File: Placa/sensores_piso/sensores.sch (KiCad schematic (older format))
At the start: 10 parts, among them P1 CONN_8X2, U1 CNY70, U2 CNY70

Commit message: arreglo placa sensores
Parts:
- removed P1: CONN_8X2, ~, symbol CONN_8X2
- removed R_sens1, R_sens2, R_sens3: 200, symbol R
- added P1: CONN_5X2, ~, symbol CONN_5X2
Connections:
- net S3+ is gone; now on net 5V: U2.C (COL)
- net Vcc is gone; now on net 5V: ??1.C (COL)
- net GND: now also RV2.3, RV3.3, P1.10
- net Vcc sensor piso izquierda: now reaches ??1.A
- net Vcc sensor piso izquierda: now also P1.4
- net Vcc sensor piso centro: now reaches U1.A
- net Vcc sensor piso centro: now also P1.6
- net Vcc sensor piso derecha: now reaches U2.A
- net Vcc sensor piso derecha: now also P1.2
- net S- renamed GND LED sensores
- net GND LED sensores: now also P1.8; no longer RV2.3, RV3.3
- net S1+ renamed 5V
- net 5V: now also P1.9
- net Sensor_Piso_Cen renamed PA1 - Sensor piso centro
- net PA1 - Sensor piso centro: now also P1.5
- net Sensor_Piso_Der renamed PA2 - Sensor piso derecha
- net PA2 - Sensor piso derecha: now also P1.1
- net Sensor_Piso_Izq renamed PA0 - Sensor piso izquierda
- net PA0 - Sensor piso izquierda: now also P1.3
- no-connect marks 8 -> 1

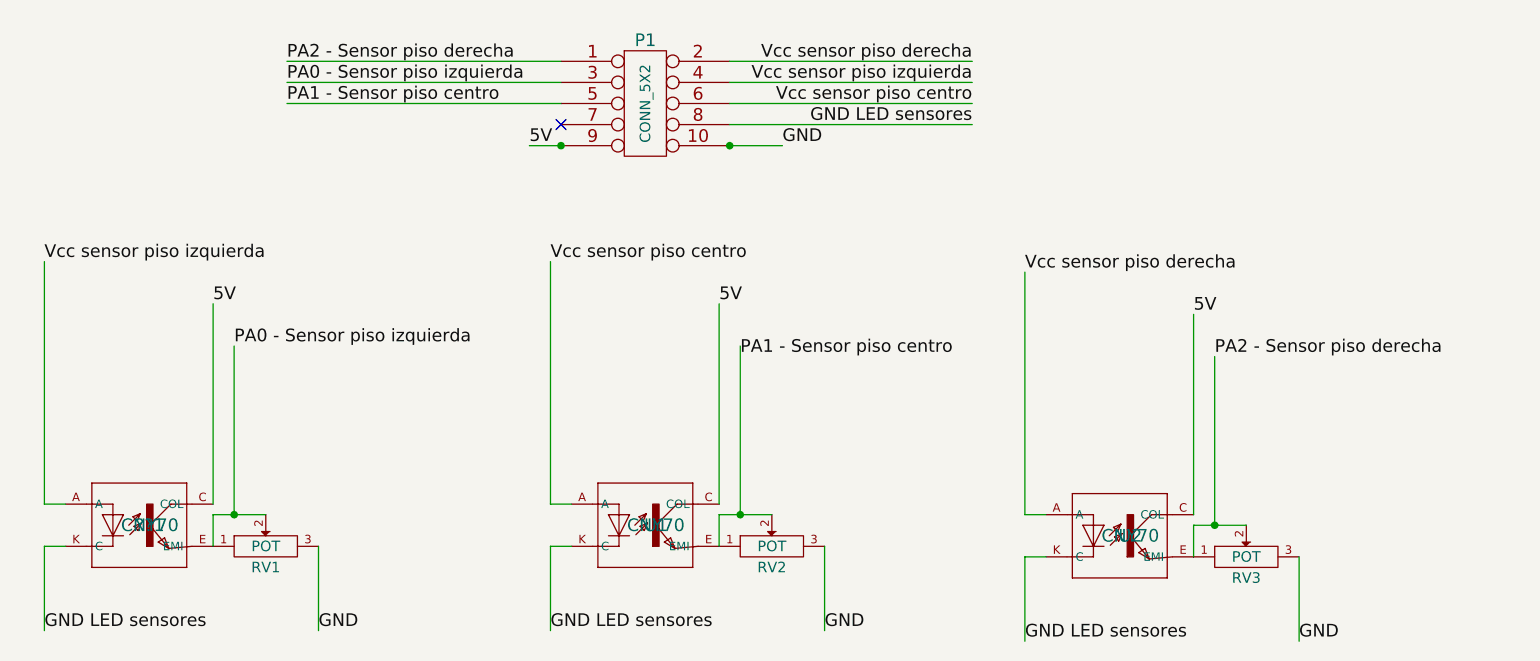
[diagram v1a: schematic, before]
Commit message: Termino y ruteo placa Sensores, Creo Gerbers de Placa de sensores y de Alimentacion.
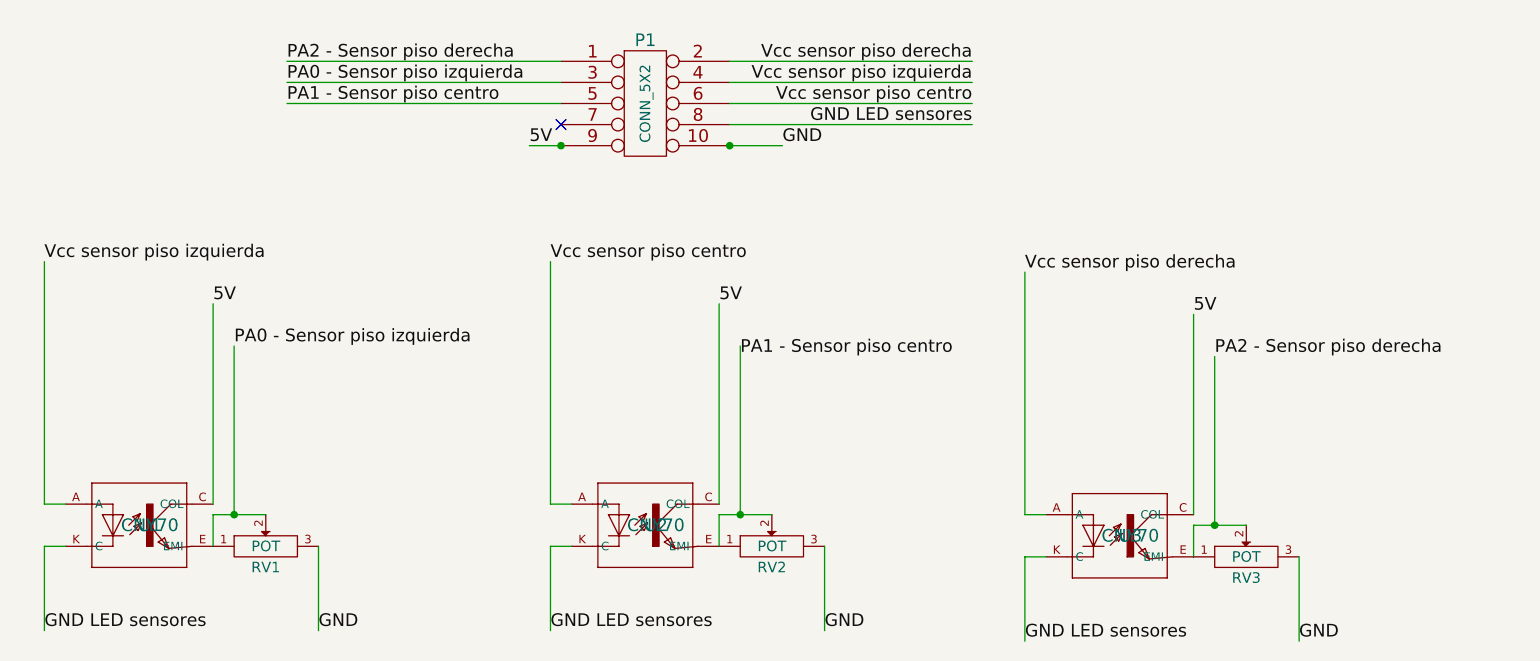
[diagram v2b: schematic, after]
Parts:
- removed U2: CNY70, symbol CNY70
- added U3: CNY70, symbol CNY70
- renumbered ??1 to U1, U1 to U2
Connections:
- net 5V: now also U3.C (COL)
- net GND LED sensores: now also U3.K (C)
- net PA2 - Sensor piso derecha: now also U3.E (EMI)
- net Vcc sensor piso derecha: now also U3.A
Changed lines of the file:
@@
 $EndComp
 $Comp
-L CNY70 ??1
+L CNY70 U1
 U 1 1 516A2AAF
 P 1750 3200
-F 0 "??1" H 1750 3200 60  0000 C CNN
+F 0 "U1" H 1750 3200 60  0000 C CNN
 F 1 "CNY70" H 1750 3200 60  0000 C CNN
 F 2 "" H 1750 3200 60  0001 C CNN
@@
 $EndComp
 $Comp
-L CNY70 U1
+L CNY70 U2
 U 1 1 51A284FA
 P 4150 3200
-F 0 "U1" H 4150 3200 60  0000 C CNN
+F 0 "U2" H 4150 3200 60  0000 C CNN
 F 1 "CNY70" H 4150 3200 60  0000 C CNN
 F 2 "" H 4150 3200 60  0001 C CNN
@@
 F 3 "" H 6950 3350 60  0001 C CNN
 	1    6950 3350
-	1    0    0    -1
-$EndComp
-$Comp
-L CNY70 U2
-U 1 1 51A2851A
-P 6400 3250
-F 0 "U2" H 6400 3250 60  0000 C CNN
-F 1 "CNY70" H 6400 3250 60  0000 C CNN
-F 2 "" H 6400 3250 60  0001 C CNN
-F 3 "" H 6400 3250 60  0001 C CNN
-	1    6400 3250
 	1    0    0    -1
 $EndComp
@@
 Wire Wire Line
 	7200 3350 7200 3750
+$Comp
+L CNY70 U3
+U 1 1 51A299A4
+P 6400 3250
+F 0 "U3" H 6400 3250 60  0000 C CNN
+F 1 "CNY70" H 6400 3250 60  0000 C CNN
+F 2 "" H 6400 3250 60  0001 C CNN
+F 3 "" H 6400 3250 60  0001 C CNN
+	1    6400 3250
+	1    0    0    -1
+$EndComp
 $EndSCHEMATC
